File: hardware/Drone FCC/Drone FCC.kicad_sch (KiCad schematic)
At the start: 5 parts, among them J23 105017-0001

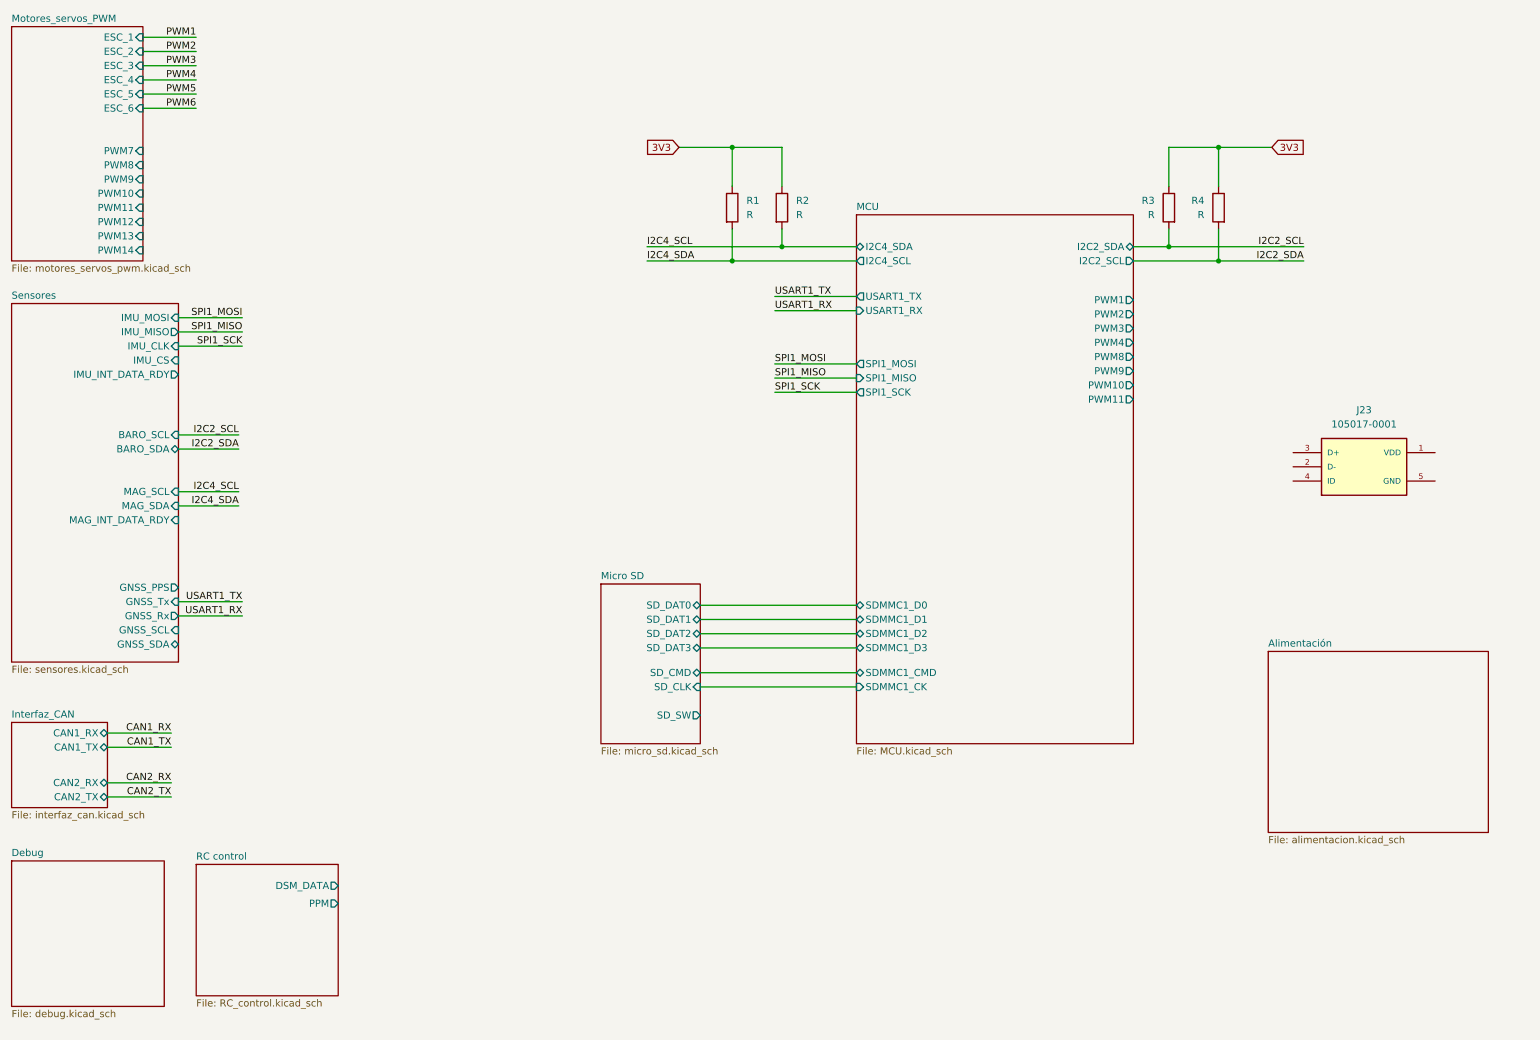
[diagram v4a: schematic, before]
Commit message: add usb TVS diodes and mcu pin assignment
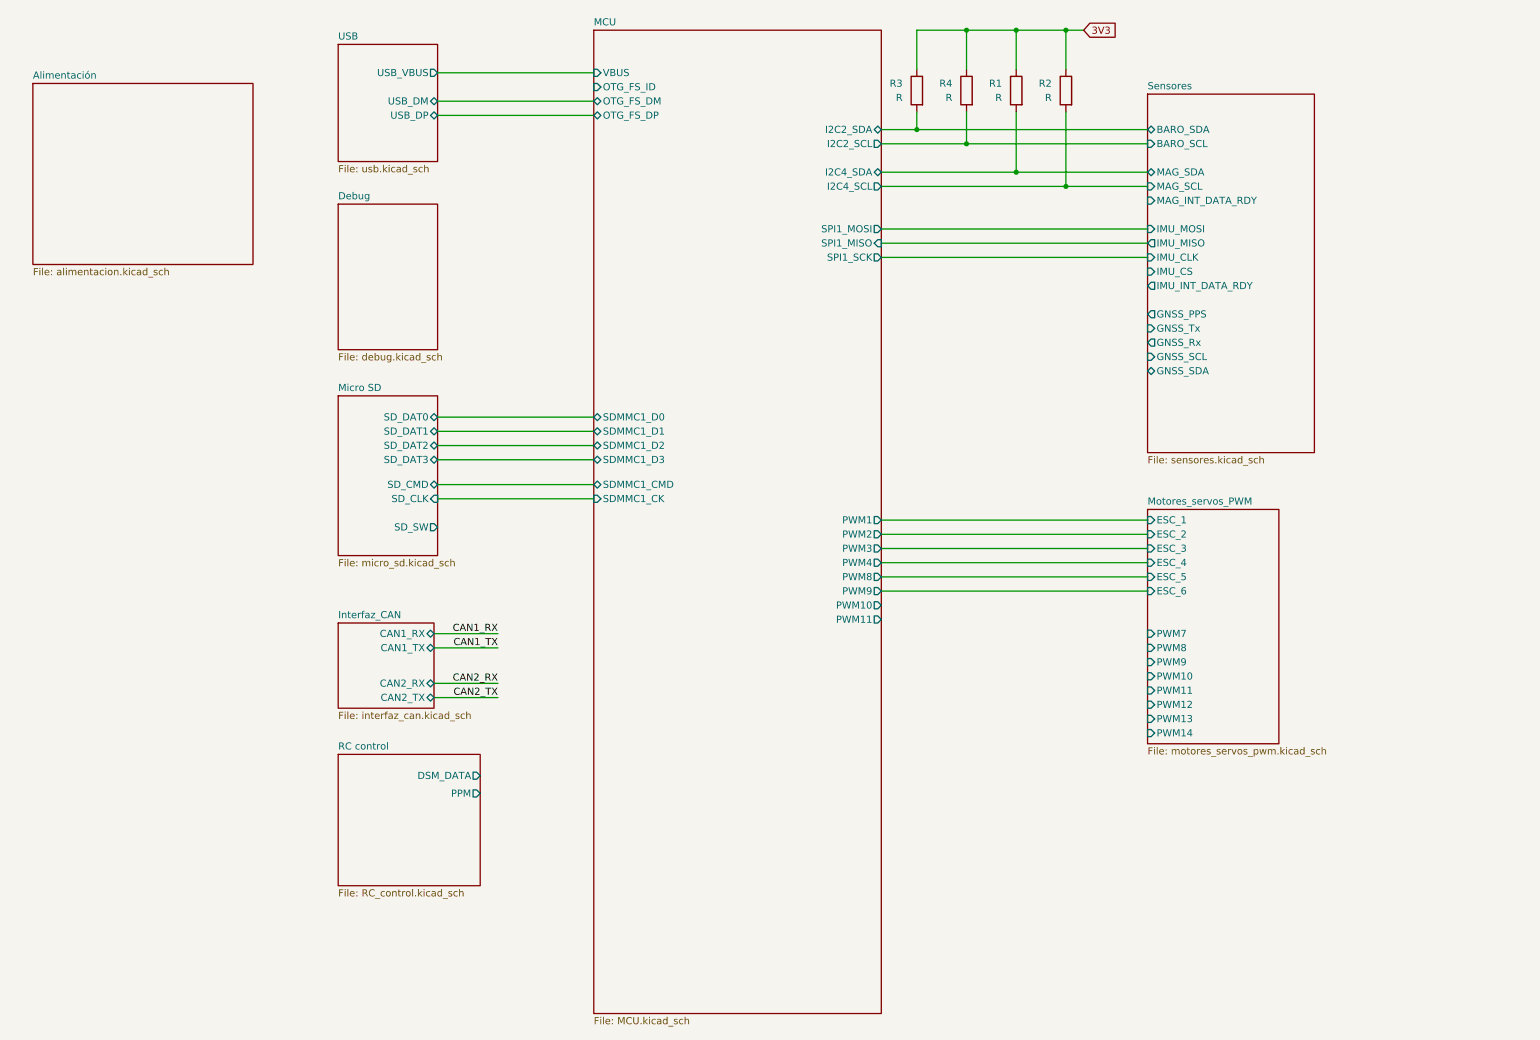
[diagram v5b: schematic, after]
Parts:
- removed J23: 105017-0001, 105017-0001:MOLEX_105017-0001, symbol 105017-0001:105017-0001
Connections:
- net I2C2_SCL renamed MCU/I2C2_SDA
- net I2C2_SDA renamed MCU/I2C2_SCL
- net I2C4_SCL renamed MCU/I2C4_SCL
- net I2C4_SDA renamed MCU/I2C4_SDA
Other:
- added sheet USB (usb.kicad_sch)
- sheet MCU ports: added OTG_FS_DM, OTG_FS_DP, OTG_FS_ID, VBUS; removed USART1_RX, USART1_TX
- moved on the sheet: R1, R2, R3, R4

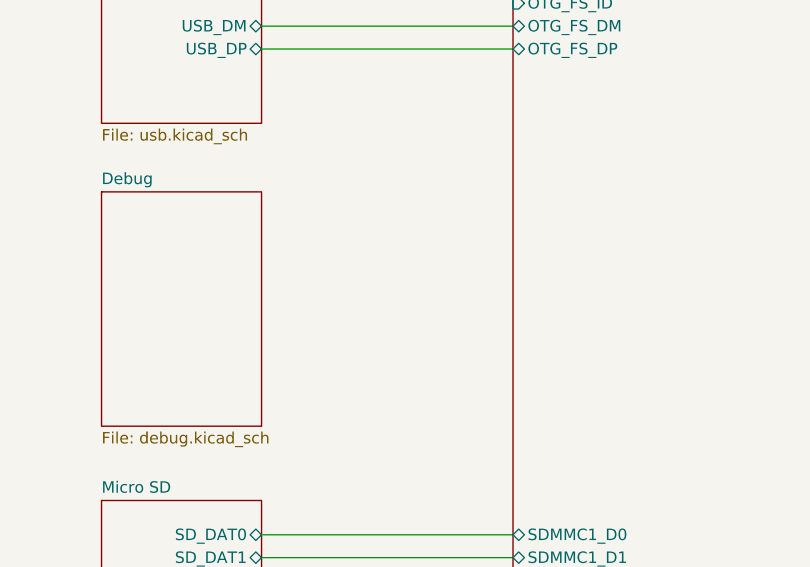
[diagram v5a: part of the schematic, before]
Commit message: finish SWD functional schematic
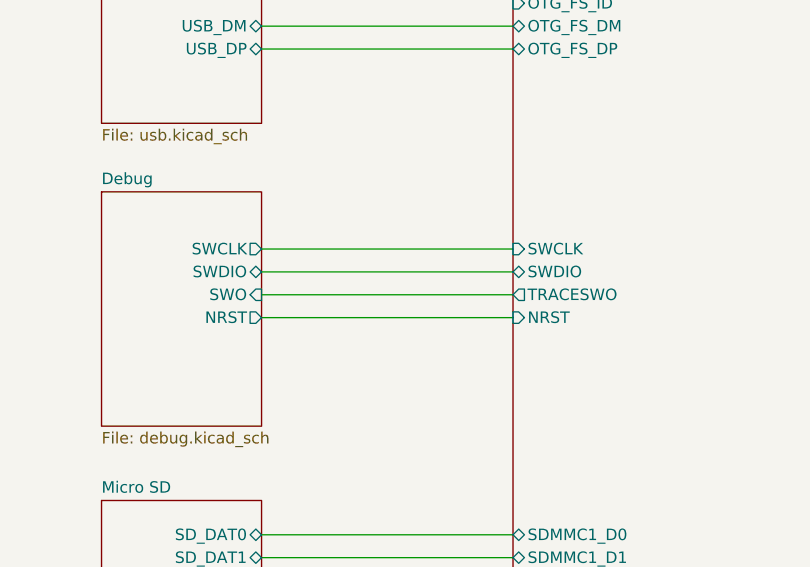
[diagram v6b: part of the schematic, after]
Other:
- sheet Debug ports: added NRST, SWCLK, SWDIO, SWO; removed none
- sheet MCU ports: added NRST, SWCLK, SWDIO, TRACESWO; removed none
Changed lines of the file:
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@@
+    (stroke (width 0) (type default) (color 0 0 0 0))
+  )
+  (wire (pts (xy 90.805 62.23) (xy 118.745 62.23))
     (stroke (width 0) (type default) (color 0 0 0 0))
   )
@@
     (stroke (width 0) (type default) (color 0 0 0 0))
   )
+  (wire (pts (xy 90.805 57.15) (xy 118.745 57.15))
+    (stroke (width 0) (type default) (color 0 0 0 0))
+  )
   (wire (pts (xy 90.17 127.635) (xy 101.6 127.635))
     (stroke (width 0) (type default) (color 0 0 0 0))
@@
     (stroke (width 0) (type default) (color 0 0 0 0))
   )
+  (wire (pts (xy 90.805 54.61) (xy 118.745 54.61))
+    (stroke (width 0) (type default) (color 0 0 0 0))
+  )
   (wire (pts (xy 90.805 88.9) (xy 118.745 88.9))
     (stroke (width 0) (type default) (color 0 0 0 0))
@@
   )
   (wire (pts (xy 170.18 109.855) (xy 217.805 109.855))
+    (stroke (width 0) (type default) (color 0 0 0 0))
+  )
+  (wire (pts (xy 90.805 59.69) (xy 118.745 59.69))
     (stroke (width 0) (type default) (color 0 0 0 0))
   )
@@
       (effects (font (size 1.27 1.27)) (justify left top))
     )
+    (pin "SWCLK" output (at 90.805 54.61 0)
+      (effects (font (size 1.27 1.27)) (justify right))
+    )
+    (pin "SWDIO" bidirectional (at 90.805 57.15 0)
+      (effects (font (size 1.27 1.27)) (justify right))
+    )
+    (pin "SWO" input (at 90.805 59.69 0)
+      (effects (font (size 1.27 1.27)) (justify right))
+    )
+    (pin "NRST" output (at 90.805 62.23 0)
+      (effects (font (size 1.27 1.27)) (justify right))
+    )
   )
   (sheet (at 118.745 17.145) (size 51.435 175.895) (fields_autoplaced)
@@
     )
     (pin "VBUS" input (at 118.745 24.765 180)
+      (effects (font (size 1.27 1.27)) (justify left))
+    )
+    (pin "TRACESWO" output (at 118.745 59.69 180)
+      (effects (font (size 1.27 1.27)) (justify left))
+    )
+    (pin "SWDIO" bidirectional (at 118.745 57.15 180)
+      (effects (font (size 1.27 1.27)) (justify left))
+    )
+    (pin "SWCLK" input (at 118.745 54.61 180)
+      (effects (font (size 1.27 1.27)) (justify left))
+    )
+    (pin "NRST" input (at 118.745 62.23 180)
       (effects (font (size 1.27 1.27)) (justify left))
     )
@@
       (reference "#PWR0117") (unit 1) (value "GND") (footprint "")
     )
-    (path "/79e0599a-7098-4a96-b5a2-c7f60ed6c34f/60d2136a-a5f2-46f4-98c8-e7f4034c2594"
+    (path "/79e0599a-7098-4a96-b5a2-c7f60ed6c34f/70077f0f-b2cc-45a9-9055-36380a521b2a"
       (reference "#PWR0118") (unit 1) (value "GND") (footprint "")
     )
@@
       (reference "#PWR0121") (unit 1) (value "GND") (footprint "")
     )
+    (path "/7aefb805-1ee8-4c99-a02a-c3e1e1ca7ccb/0c849357-bfca-4211-a06d-eb82fa2e698f"
+      (reference "#PWR0123") (unit 1) (value "GND") (footprint "")
+    )
+    (path "/7aefb805-1ee8-4c99-a02a-c3e1e1ca7ccb/90e9a6ac-e932-494b-8310-4c3b9110753e"
+      (reference "#PWR0124") (unit 1) (value "GND") (footprint "")
+    )
     (path "/ed1e96fa-b1be-4881-8dac-8041c949f89e/0abf3cd6-cb8f-438c-96bd-6f4cb0dbe57c"
-      (reference "#PWR?") (unit 1) (value "GND") (footprint "")
-    )
-    (path "/7aefb805-1ee8-4c99-a02a-c3e1e1ca7ccb/0c849357-bfca-4211-a06d-eb82fa2e698f"
-      (reference "#PWR?") (unit 1) (value "GND") (footprint "")
-    )
-    (path "/7aefb805-1ee8-4c99-a02a-c3e1e1ca7ccb/90e9a6ac-e932-494b-8310-4c3b9110753e"
-      (reference "#PWR?") (unit 1) (value "GND") (footprint "")
+      (reference "#PWR0125") (unit 1) (value "GND") (footprint "")
     )
     (path "/ed1e96fa-b1be-4881-8dac-8041c949f89e/a8699ada-c75e-4d35-9128-0ca2f54bc386"
-      (reference "#PWR?") (unit 1) (value "GND") (footprint "")
+      (reference "#PWR0126") (unit 1) (value "GND") (footprint "")
     )
     (path "/2dea4649-a03b-4105-a448-fdfd58cb624b/7430465c-9d48-4f87-807f-b7d872f0d403"
@@
     )
     (path "/7aefb805-1ee8-4c99-a02a-c3e1e1ca7ccb/9c7f0ec9-e771-43fe-997d-ae2bb4963586"
-      (reference "C?") (unit 1) (value "100nF") (footprint "")
+      (reference "C7") (unit 1) (value "100nF") (footprint "")
     )
     (path "/7aefb805-1ee8-4c99-a02a-c3e1e1ca7ccb/b7ae2086-d714-48d0-91ce-9cbf32d63163"
-      (reference "C?") (unit 1) (value "1uF") (footprint "")
+      (reference "C8") (unit 1) (value "1uF") (footprint "")
     )
     (path "/2dea4649-a03b-4105-a448-fdfd58cb624b/1ada52bf-3160-4b2e-8e93-ed65b64dff92"
@@
       (reference "J21") (unit 1) (value "Micro_SD_Card_Det_Hirose_DM3AT") (footprint "DM3AT-SF-PEJM5:HRS_DM3AT-SF-PEJM5")
     )
-    (path "/79e0599a-7098-4a96-b5a2-c7f60ed6c34f/6e75ea62-60ae-42b3-bd38-71ccbf1d1f4d"
-      (reference "J22") (unit 1) (value "Conn_02x05_Odd_Even") (footprint "FTSH-105-01-F-DV-K-TR:SAMTEC_FTSH-105-01-F-DV-P-TR")
+    (path "/79e0599a-7098-4a96-b5a2-c7f60ed6c34f/8f7d07ad-b85a-4ca2-8874-23bb139ed72d"
+      (reference "J22") (unit 1) (value "Conn_02x03_Counter_Clockwise") (footprint "Connector_PinHeader_2.54mm:PinHeader_2x03_P2.54mm_Vertical")
     )
     (path "/2e02b919-519b-4cae-a6fb-682f19bf0ab7/6299bbba-da38-4b1d-aee3-1b5562e402d2"
       (reference "J24") (unit 1) (value "DSM Spektrum JST") (footprint "B3B-ZR-SM4-TF(LF)(SN):JST-B3B-ZR-SM4-TFLFSN-0-0-MFG")
     )
-    (path "/79e0599a-7098-4a96-b5a2-c7f60ed6c34f/9888d426-3a1e-46c9-905c-aefc408436a3"
-      (reference "J25") (unit 1) (value "Conn_02x02_Counter_Clockwise") (footprint "")
+    (path "/ed1e96fa-b1be-4881-8dac-8041c949f89e/3334d295-191e-4b5f-8306-d88a7ed5ee90"
+      (reference "J25") (unit 1) (value "105017-0001") (footprint "105017-0001:MOLEX_105017-0001")
     )
     (path "/2e02b919-519b-4cae-a6fb-682f19bf0ab7/a62587f8-37d8-4b1d-96f5-2656816cd2dc"
@@
       (reference "J28") (unit 1) (value "PM02 PixHawk") (footprint "Connector_Hirose:Hirose_DF13C_CL535-0406-3-51_1x06-1MP_P1.25mm_Vertical")
     )
-    (path "/ed1e96fa-b1be-4881-8dac-8041c949f89e/3334d295-191e-4b5f-8306-d88a7ed5ee90"
-      (reference "J?") (unit 1) (value "105017-0001") (footprint "105017-0001:MOLEX_105017-0001")
-    )
     (path "/9bc65728-e237-4f6c-82eb-0920dd4372d2"
       (reference "R1") (unit 1) (value "R") (footprint "")
@@
       (reference "R10") (unit 1) (value "10k") (footprint "")
     )
+    (path "/7aefb805-1ee8-4c99-a02a-c3e1e1ca7ccb/411bec58-89fa-4cb5-b578-a5241374e3d2"
+      (reference "R11") (unit 1) (value "33k") (footprint "")
+    )
     (path "/7aefb805-1ee8-4c99-a02a-c3e1e1ca7ccb/148a42d0-1f1d-476a-b3c5-4f586adf117b"
-      (reference "R?") (unit 1) (value "82k") (footprint "")
-    )
-    (path "/7aefb805-1ee8-4c99-a02a-c3e1e1ca7ccb/411bec58-89fa-4cb5-b578-a5241374e3d2"
-      (reference "R?") (unit 1) (value "33k") (footprint "")
+      (reference "R12") (unit 1) (value "82k") (footprint "")
     )
     (path "/2dea4649-a03b-4105-a448-fdfd58cb624b/526c1ffa-b5c3-4a19-b2e6-f432001e1abc"
@@
     )
     (path "/ed1e96fa-b1be-4881-8dac-8041c949f89e/b6479ba7-9645-4aa6-8008-d852f1df1552"
-      (reference "U?") (unit 1) (value "USBLC6-2SC6") (footprint "Package_TO_SOT_SMD:SOT-23-6")
-    )
-  )
+      (reference "U7") (unit 1) (value "USBLC6-2SC6") (footprint "Package_TO_SOT_SMD:SOT-23-6")
+    )
+  )
